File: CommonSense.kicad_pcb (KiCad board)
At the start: 2 copper layers, 34 x 24 mm, 31 parts, among them J1 Conn_02x04_Counter_Clockwise, U1 NRF52810-QFAA-R7, U2 SHT41-AD1B-R2, Y1 ECS-.327-12.5-12R-TR, Y2 ABM11W-32.0000MHZ-7-D1X-T3

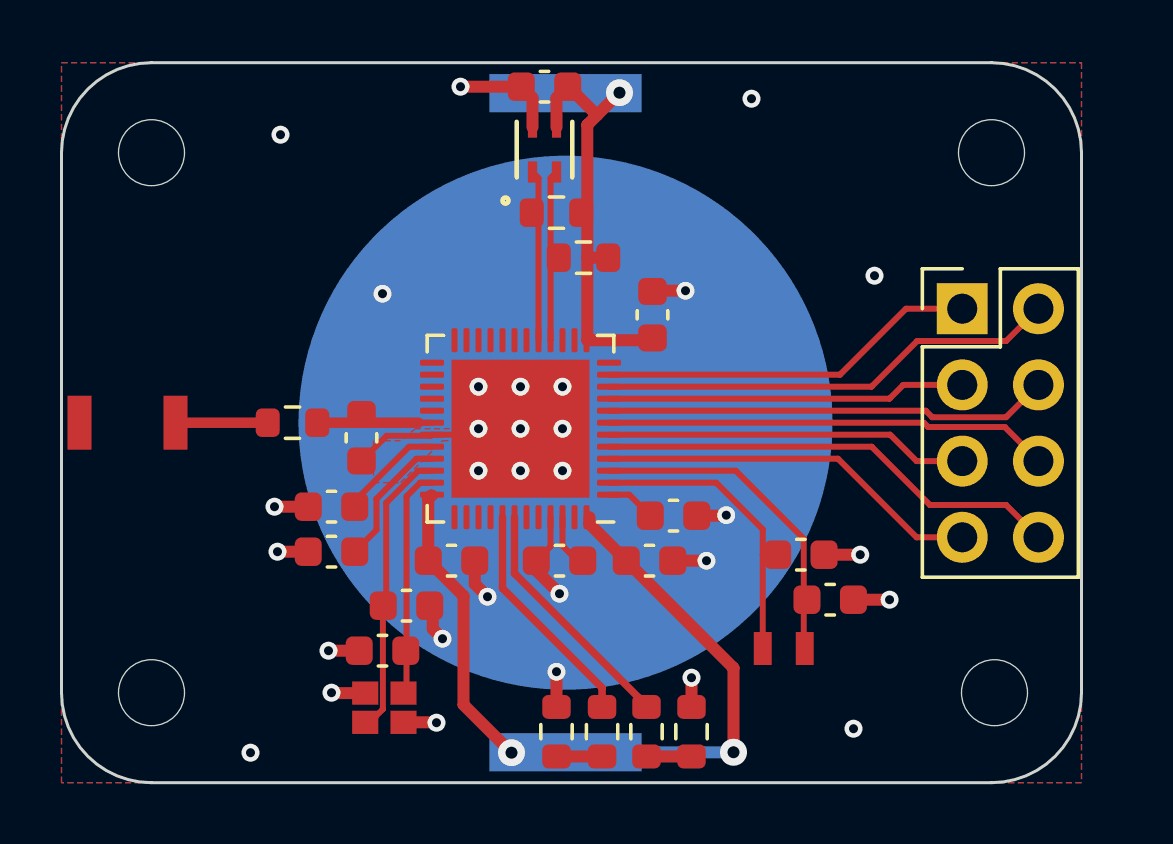
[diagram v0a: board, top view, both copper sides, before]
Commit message: Add 1x2 pin headers for power and I2C
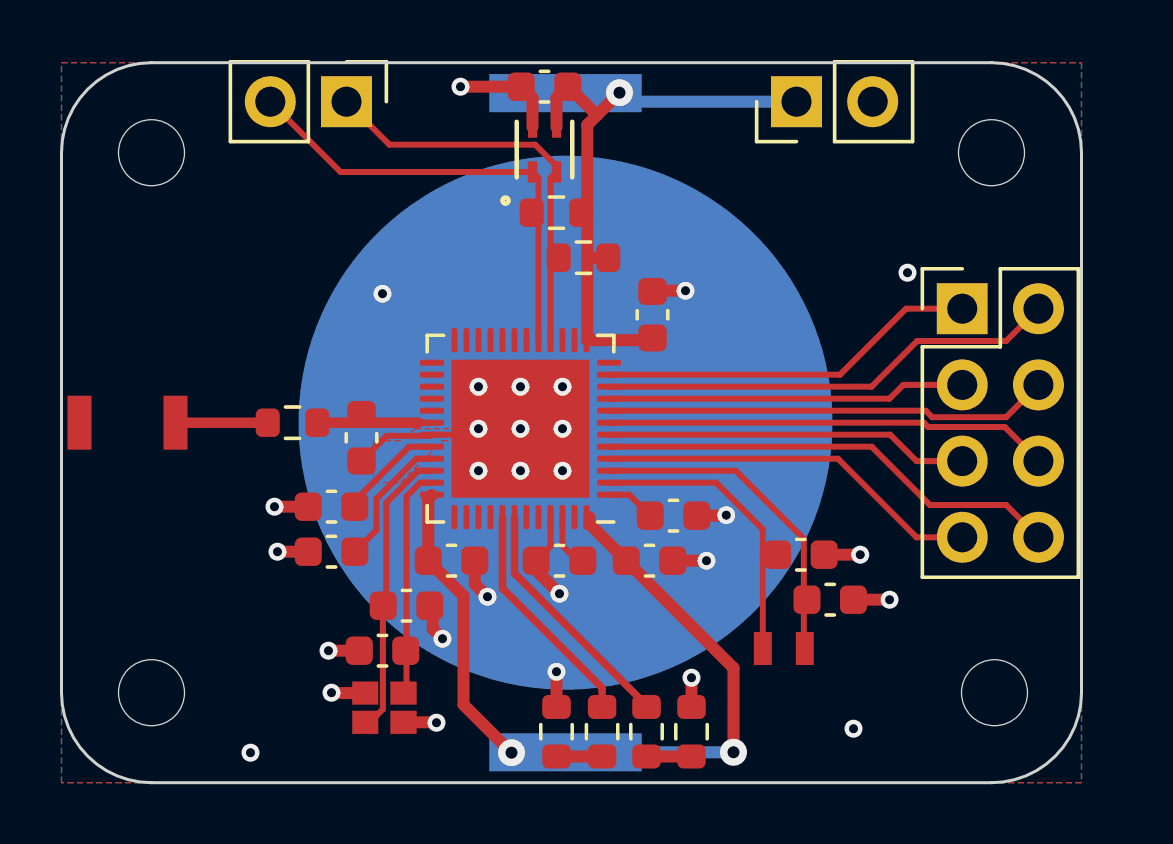
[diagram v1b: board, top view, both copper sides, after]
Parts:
- added J2: Conn_01x02, Connector_PinHeader_2.54mm:PinHeader_1x02_P2.54mm_Vertical, F.Cu at (160.5, 57.3)
- added J3: Conn_01x02, Connector_PinHeader_2.54mm:PinHeader_1x02_P2.54mm_Vertical, F.Cu at (145.5, 57.3)
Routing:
- net /SDA: track 5.69 -> 15.4 mm
- net /SCL: track 5.69 -> 13.8 mm
- net +3V3: track 39.7 -> 47.5 mm
- net GND: vias 31 -> 29

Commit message: Position i2c and power bit headers close to other header; Add text to silk screen
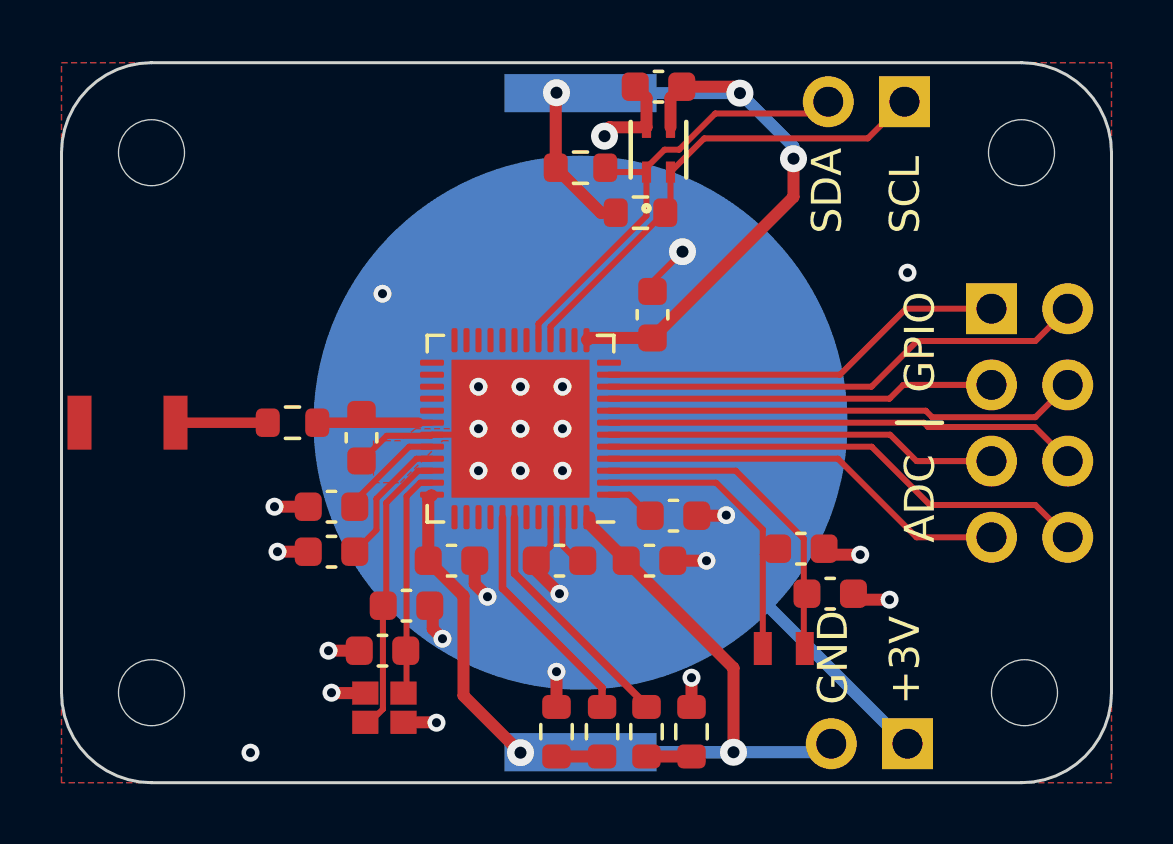
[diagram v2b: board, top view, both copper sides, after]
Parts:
- moved J2 21.7 mm to (164.2, 78.7), turned to -90 degrees
- moved J3 18.6 mm to (164.1, 57.3)
- moved U2 3.80 mm to (155.9, 58.9)
- moved C13 3.80 mm to (155.9, 56.8)
- moved R3 2.42 mm to (155.3, 61.0), turned to 180 degrees
- moved R4 1.70 mm to (153.3, 59.5), turned to 0 degrees
- moved H3 1.00 mm to (168.0, 59.0)
- moved H4 1.00 mm to (168.1, 77.0)
- moved J1 0.97 mm to (167.0, 64.2)
- moved BT1 0.50 mm to (153.3, 68.0)
- moved C1 0.20 mm to (160.6, 72.2)
- moved C2 0.20 mm to (161.6, 73.7)
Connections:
- J2 pad 1: +3V3 -> GND
- J2 pad 2: GND -> +3V3
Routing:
- net GND: track 26.8 -> 42.0 mm, vias 29 -> 28
- net +3V3: track 47.5 -> 60.4 mm, vias 3 -> 5
- net /SCL: track 13.8 -> 16.0 mm
- net /AIN3: track 14.9 -> 15.8 mm
- net /P0.09: track 12.7 -> 13.7 mm
- net /P0.08: track 15.4 -> 16.4 mm
- net /P0.07: track 12.0 -> 12.9 mm
- net /P0.06: track 14.9 -> 15.8 mm
- net /AIN1: track 15.6 -> 16.5 mm
- net /AIN0: track 12.9 -> 13.8 mm
- net /AIN2: track 12.1 -> 13.1 mm
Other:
- board size 34 x 24 mm -> 35 x 24 mm
- board text added: "+3V"
- board text added: "ADC"
- board text added: "GND"
- board text added: "GPIO"
- board text added: "SCL"
- board text added: "SDA"

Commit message: Move around vias
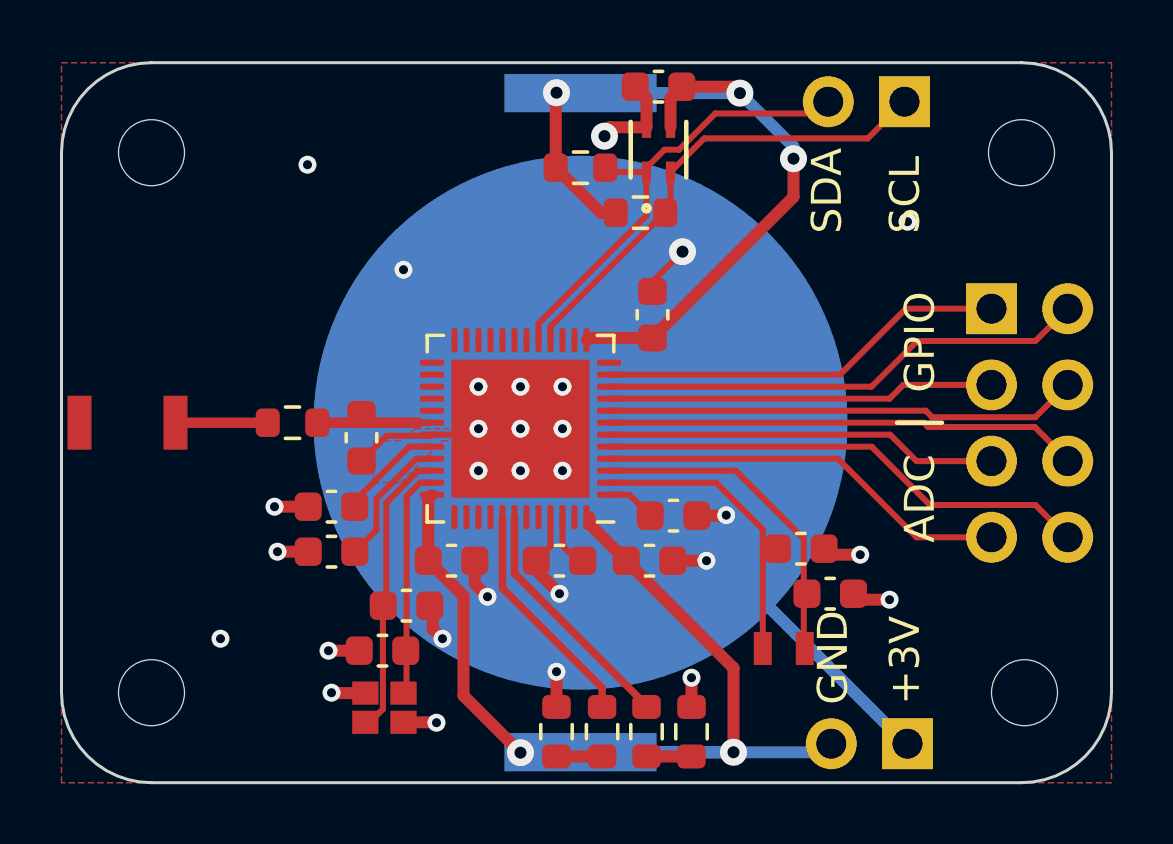
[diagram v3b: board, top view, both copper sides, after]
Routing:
- net GND: vias 28 -> 29
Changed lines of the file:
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@@
   (via (at 157.5 72.6) (size 0.6) (drill 0.3) (layers "F.Cu" "B.Cu") (net 3))
   (via (at 151.3 69.6) (size 0.6) (drill 0.3) (layers "F.Cu" "B.Cu") (net 3))
-  (via (at 142.3 79) (size 0.6) (drill 0.3) (layers "F.Cu" "B.Cu") (net 3))
+  (via (at 141.3 75.2) (size 0.6) (drill 0.3) (layers "F.Cu" "B.Cu") (net 3))
   (via (at 158.15864 71.08272) (size 0.6) (drill 0.3) (layers "F.Cu" "B.Cu") (net 3))
-  (via (at 164.2 63) (size 0.6) (drill 0.3) (layers "F.Cu" "B.Cu") (net 3))
+  (via (at 164.2 61.3) (size 0.6) (drill 0.3) (layers "F.Cu" "B.Cu") (net 3))
   (via (at 144.9 75.6) (size 0.6) (drill 0.3) (layers "F.Cu" "B.Cu") (net 3))
   (via (at 157 76.5) (size 0.6) (drill 0.3) (layers "F.Cu" "B.Cu") (net 3))
@@
   (via (at 149.9 66.8) (size 0.6) (drill 0.3) (layers "F.Cu" "B.Cu") (net 3))
   (via (at 149.9 69.6) (size 0.6) (drill 0.3) (layers "F.Cu" "B.Cu") (net 3))
-  (via (at 146.7 63.7) (size 0.6) (drill 0.3) (layers "F.Cu" "B.Cu") (net 3))
+  (via (at 147.4 62.9) (size 0.6) (drill 0.3) (layers "F.Cu" "B.Cu") (net 3))
   (via (at 150.2 73.8) (size 0.6) (drill 0.3) (layers "F.Cu" "B.Cu") (net 3))
+  (via (at 144.2 59.4) (size 0.6) (drill 0.3) (layers "F.Cu" "B.Cu") (net 3))
   (via (at 163.60245 73.899999) (size 0.6) (drill 0.3) (layers "F.Cu" "B.Cu") (net 3))
   (via (at 154.1 58.4485) (size 0.9) (drill 0.4) (layers "F.Cu" "B.Cu") (net 3))

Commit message: Add SWD connector; Add text on silkscreen
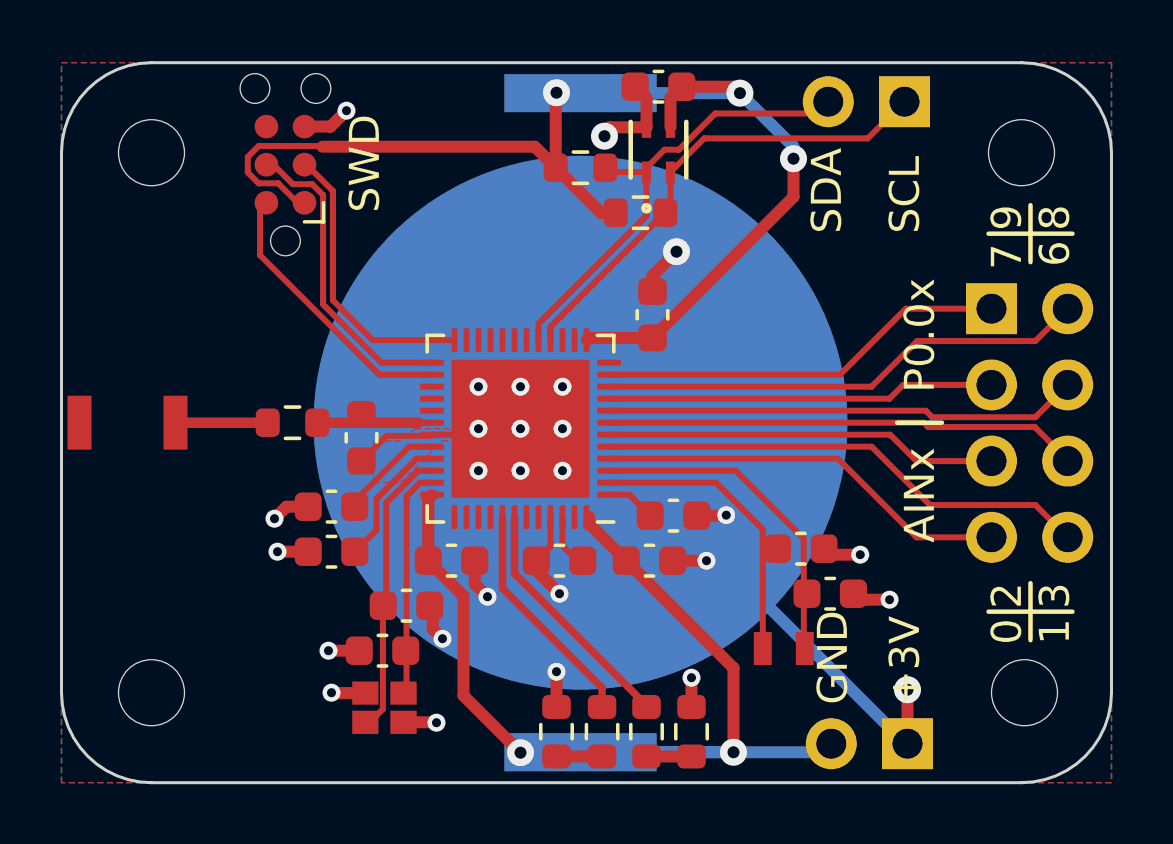
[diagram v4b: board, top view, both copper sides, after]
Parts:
- added J5: Conn_ARM_SWD_TagConnect_TC2030-NL, Connector:Tag-Connect_TC2030-IDC-NL_2x03_P1.27mm_Vertical, F.Cu at (143.5, 59.4)
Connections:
- U1 pad 24: /RESET -> /NRESET
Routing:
- net +3V3: track 60.4 -> 73.9 mm
- net /SWDCLK: track 0.00 -> 10.4 mm
- net /NRESET: track 0.00 -> 9.56 mm
- net /SWDIO: track 0.00 -> 9.22 mm
- net GND: track 42.0 -> 45.5 mm, vias 29 -> 27
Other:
- board text added: "0"
- board text added: "1"
- board text added: "2"
- board text added: "3"
- board text added: "6"
- board text added: "7"
- board text added: "8"
- board text added: "9"
- board text added: "AINx"
- board text added: "CR2032"
- board text added: "P0.0x"
- board text added: "SWD"
- board text removed: "ADC"
- board text removed: "GPIO"
